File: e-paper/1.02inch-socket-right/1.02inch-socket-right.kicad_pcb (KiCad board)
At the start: 2 copper layers, 12 x 2 mm, 7 parts

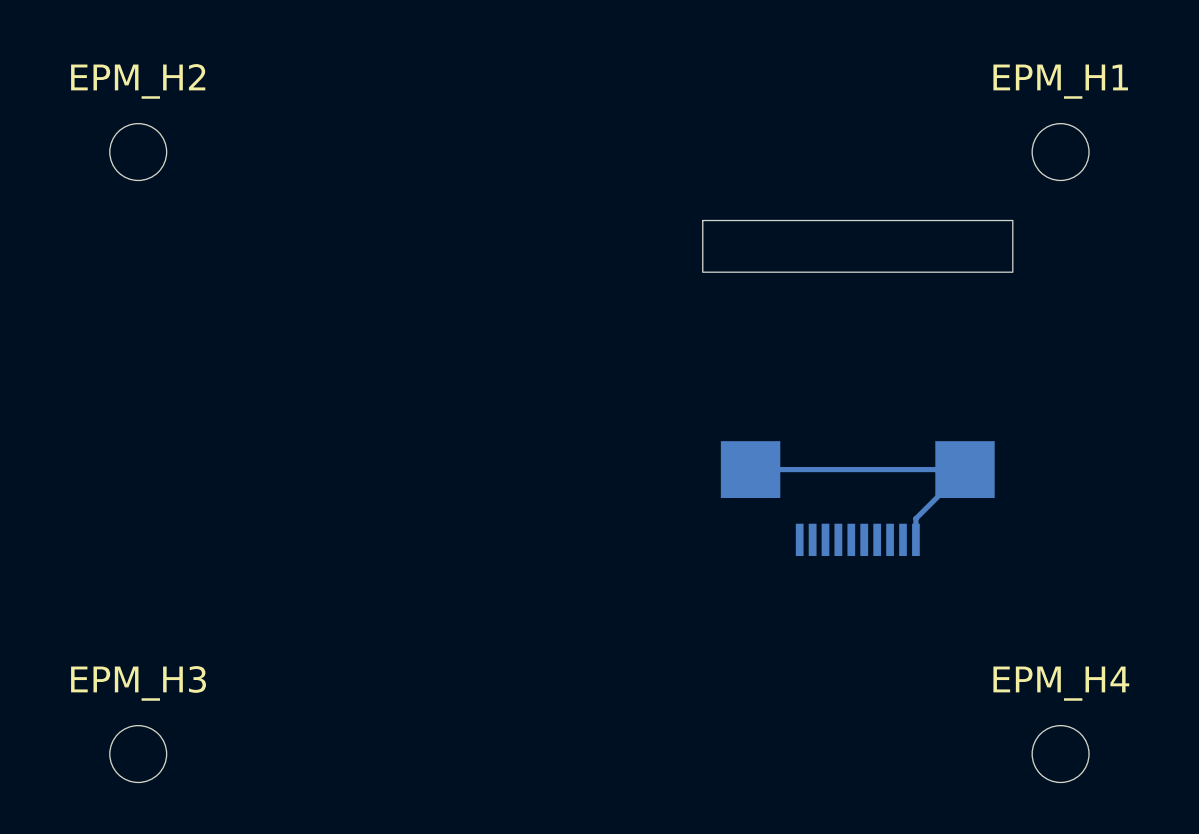
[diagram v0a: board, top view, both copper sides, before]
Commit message: add 14500 battery
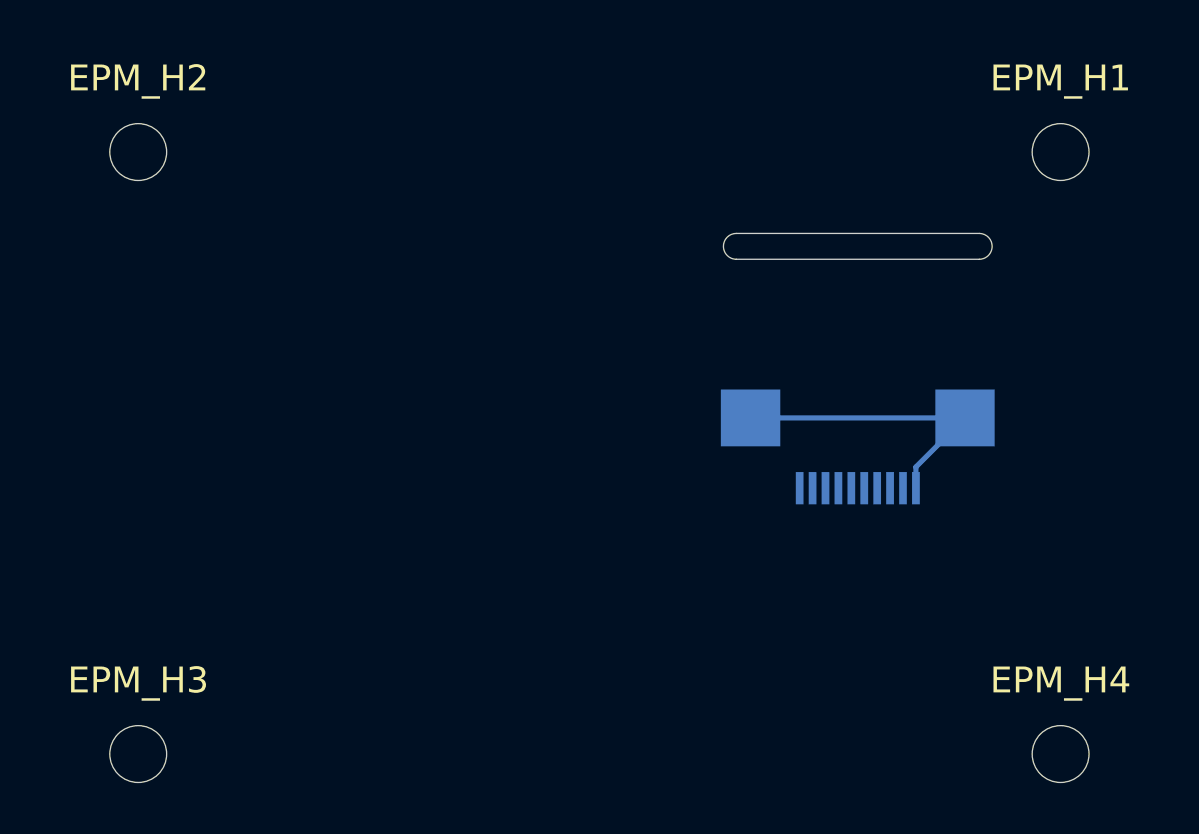
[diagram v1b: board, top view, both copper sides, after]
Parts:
- moved EPM_FPC1 2.00 mm to (10.0, 0.00)
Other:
- board size 12 x 2 mm -> 10.4 x 1 mm
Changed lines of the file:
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@@
 		(sheetfile "1.02inch-socket-right.kicad_sch")
 		(attr smd exclude_from_bom)
-		(fp_rect
-			(start -6 -1)
-			(end 6 1)
+		(fp_line
+			(start -4.7 -0.5)
+			(end 4.7 -0.5)
 			(stroke
 				(width 0.05)
-				(type solid)
-			)
-			(fill no)
+				(type default)
+			)
 			(layer "Edge.Cuts")
+		)
+		(fp_line
+			(start 4.7 0.5)
+			(end -4.7 0.5)
+			(stroke
+				(width 0.05)
+				(type default)
+			)
+			(layer "Edge.Cuts")
+		)
+		(fp_arc
+			(start -4.7 0.5)
+			(mid -5.2 0)
+			(end -4.7 -0.5)
+			(stroke
+				(width 0.05)
+				(type solid)
+			)
+			(layer "Edge.Cuts")
+		)
+		(fp_arc
+			(start 4.7 -0.5)
+			(mid 5.2 0)
+			(end 4.7 0.5)
+			(stroke
+				(width 0.05)
+				(type solid)
+			)
+			(layer "Edge.Cuts")
+		)
+		(fp_text user "${REFERENCE}"
+			(at 0 2.5 0)
+			(unlocked yes)
+			(layer "F.Fab")
+			(effects
+				(font
+					(size 1 1)
+					(thickness 0.15)
+				)
+			)
 		)
 		(embedded_fonts no)
@@
 	(footprint "ErgoCai.pretty:FPC-SMD_10P-P0.50_JS_AFD01-S10FCA-00"
 		(layer "B.Cu")
-		(at 10 2 180)
+		(at 10 0 180)
 		(property "Reference" "EPM_FPC1"
 			(at 0 5.36 0)
@@
 	)
 	(segment
-		(start 5.85 0.64)
-		(end 14.15 0.64)
+		(start 5.85 -1.36)
+		(end 14.15 -1.36)
 		(width 0.2)
 		(layer "B.Cu")
@@
 	)
 	(segment
-		(start 14.15 0.64)
-		(end 12.25 2.54)
+		(start 12.25 0.54)
+		(end 12.25 1.36)
 		(width 0.2)
 		(layer "B.Cu")
@@
 	)
 	(segment
-		(start 12.25 2.54)
-		(end 12.25 3.36)
+		(start 14.15 -1.36)
+		(end 12.25 0.54)
 		(width 0.2)
 		(layer "B.Cu")

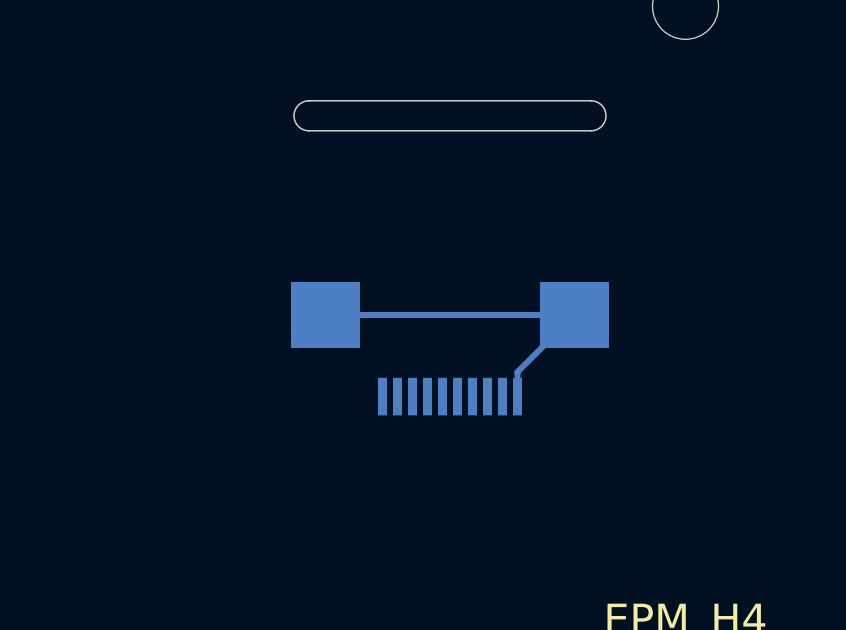
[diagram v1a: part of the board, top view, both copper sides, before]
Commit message: remove gnd link in e-paper socket
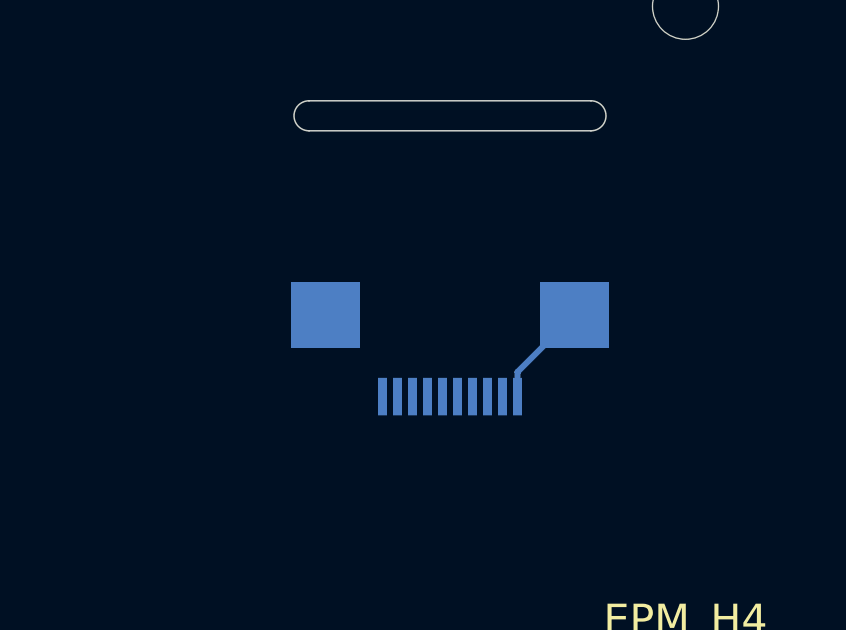
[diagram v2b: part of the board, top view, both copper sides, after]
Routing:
- net GND: track 11.8 -> 3.51 mm
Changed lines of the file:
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@@
-	)
-	(segment
-		(start 5.85 -1.36)
-		(end 14.15 -1.36)
-		(width 0.2)
-		(layer "B.Cu")
-		(net 6)
 	)
 	(segment

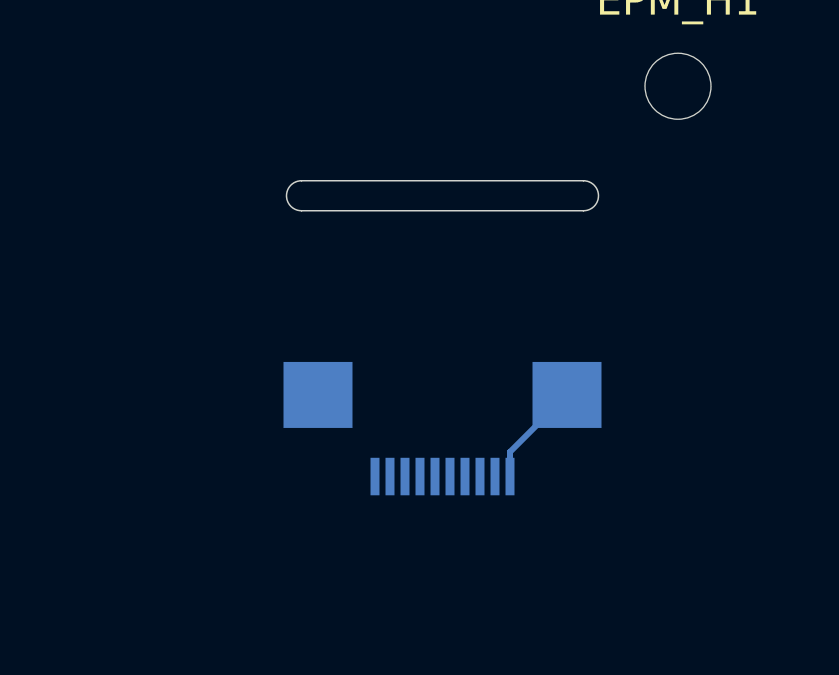
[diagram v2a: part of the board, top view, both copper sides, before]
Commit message: add joystick_fpc_hole
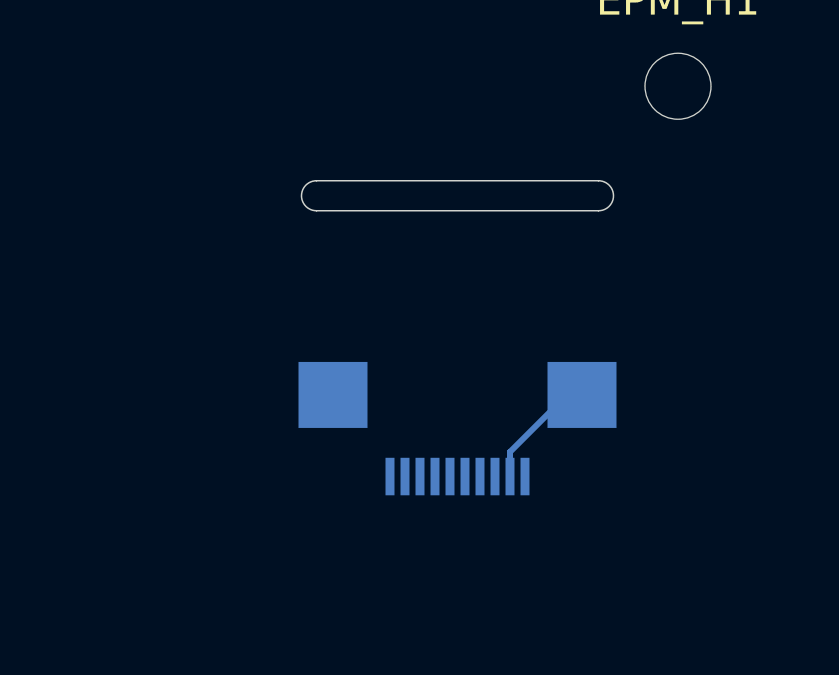
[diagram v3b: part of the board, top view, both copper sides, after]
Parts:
- moved EPM_FPC1 0.50 mm to (10.5, 0.00)
- moved EPM_GAP1 0.50 mm to (10.5, -8.00)
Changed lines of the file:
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@@
 	(footprint "ErgoCai.pretty:e-paper_1.02inch_gap"
 		(layer "F.Cu")
-		(at 10 -8)
+		(at 10.5 -8)
 		(property "Reference" "EPM_GAP1"
 			(at 0 -0.5 0)
@@
 	(footprint "ErgoCai.pretty:FPC-SMD_10P-P0.50_JS_AFD01-S10FCA-00"
 		(layer "B.Cu")
-		(at 10 0 180)
+		(at 10.5 0 180)
 		(property "Reference" "EPM_FPC1"
 			(at 0 5.36 0)
